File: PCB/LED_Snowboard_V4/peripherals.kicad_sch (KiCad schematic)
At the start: 16 parts, among them J1 Micro_SD_Card_Det_Hirose_DM3AT, U2 MPU-6050, U3 NEO-M8M

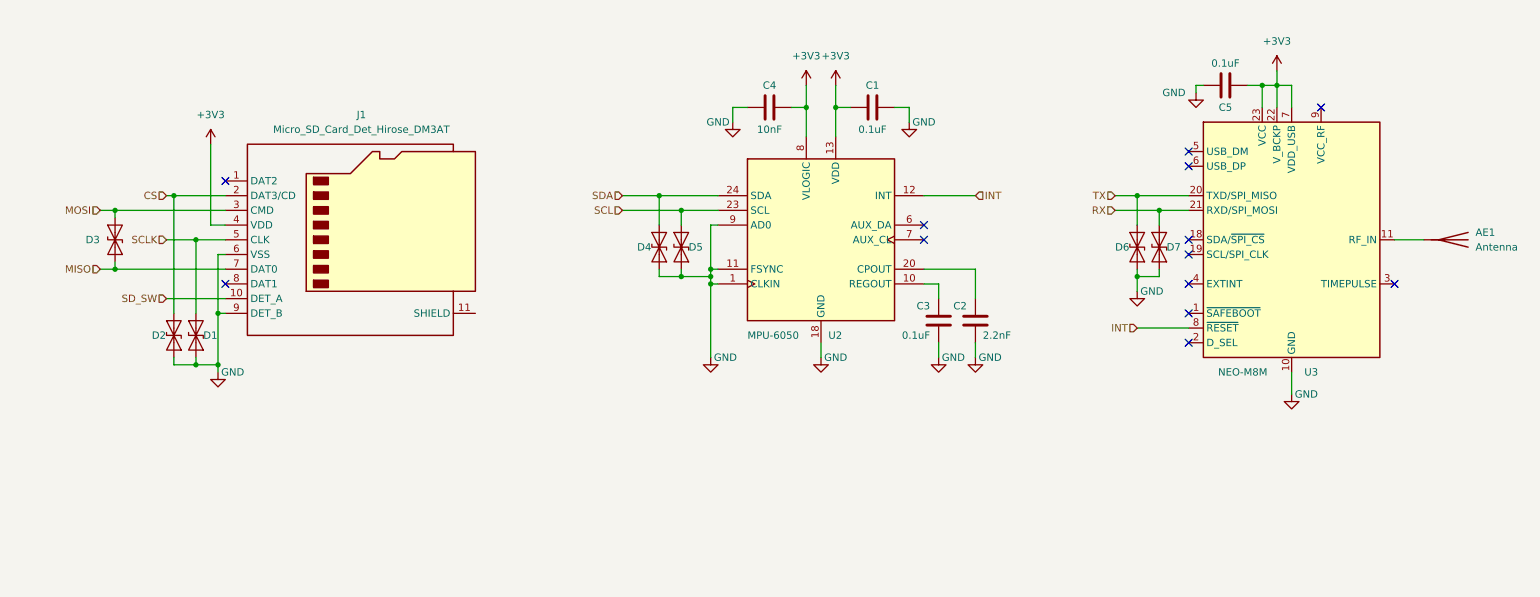
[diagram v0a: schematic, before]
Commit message: Post Review
Reviewed with Tim. need to add power line protections. settled on no battery heater for now
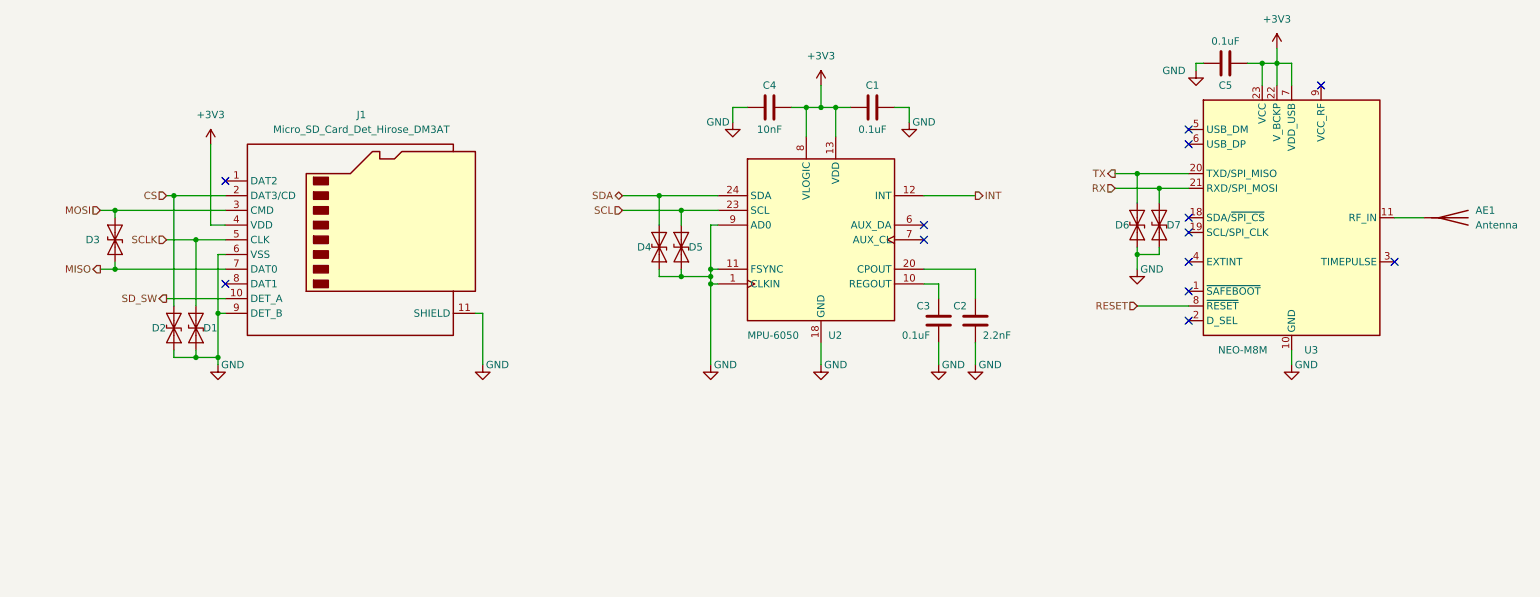
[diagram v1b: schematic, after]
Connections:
- net GND: now also J1.11 (SHIELD)
- net INT: no longer U3.8 (~{RESET})
- new net RESET: U3.8 (~{RESET})
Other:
- moved on the sheet: AE1, C5, D1, D2, D6, D7, U3

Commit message: makerfaire
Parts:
- AE1: footprint (none) -> Connector_Coaxial:U.FL_Hirose_U.FL-R-SMT-1_Vertical
- C1, C2, C3, C4, C5: footprint (none) -> Capacitor_SMD:C_0603_1608Metric_Pad1.08x0.95mm_HandSolder
- J1: footprint (none) -> Connector_Card:microSD_HC_Hirose_DM3AT-SF-PEJM5
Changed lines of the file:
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@@
       (effects (font (size 1.27 1.27)))
     )
-    (property "Footprint" "" (at 125.73 74.93 0)
+    (property "Footprint" "Connector_Card:microSD_HC_Hirose_DM3AT-SF-PEJM5" (at 125.73 74.93 0)
       (effects (font (size 1.27 1.27)) hide)
     )
@@
       (effects (font (size 1.27 1.27)))
     )
-    (property "Footprint" "" (at 148.59 68.8848 0)
+    (property "Footprint" "Capacitor_SMD:C_0603_1608Metric_Pad1.08x0.95mm_HandSolder" (at 148.59 68.8848 0)
       (effects (font (size 1.27 1.27)) hide)
     )
@@
       (effects (font (size 1.27 1.27)) (justify right))
     )
-    (property "Footprint" "" (at 179.3748 102.87 0)
+    (property "Footprint" "Capacitor_SMD:C_0603_1608Metric_Pad1.08x0.95mm_HandSolder" (at 179.3748 102.87 0)
       (effects (font (size 1.27 1.27)) hide)
     )
@@
       (effects (font (size 1.27 1.27)) (justify right))
     )
-    (property "Footprint" "" (at 173.0248 102.87 0)
+    (property "Footprint" "Capacitor_SMD:C_0603_1608Metric_Pad1.08x0.95mm_HandSolder" (at 173.0248 102.87 0)
       (effects (font (size 1.27 1.27)) hide)
     )
@@
       (effects (font (size 1.27 1.27)) (justify left))
     )
-    (property "Footprint" "" (at 262.89 88.9 0)
+    (property "Footprint" "Connector_Coaxial:U.FL_Hirose_U.FL-R-SMT-1_Vertical" (at 262.89 88.9 0)
       (effects (font (size 1.27 1.27)) hide)
     )
@@
       (effects (font (size 1.27 1.27)))
     )
-    (property "Footprint" "" (at 166.37 68.8848 0)
+    (property "Footprint" "Capacitor_SMD:C_0603_1608Metric_Pad1.08x0.95mm_HandSolder" (at 166.37 68.8848 0)
       (effects (font (size 1.27 1.27)) hide)
     )
@@
       (effects (font (size 1.27 1.27)))
     )
-    (property "Footprint" "" (at 219.71 63.1952 0)
-      (effects (font (size 1.27 1.27)) hide)
-    )
+    (property "Footprint" "Capacitor_SMD:C_0603_1608Metric_Pad1.08x0.95mm_HandSolder" (at 219.71 63.1952 0)
+      (effects (font (size 1.27 1.27)) hide)
+    )

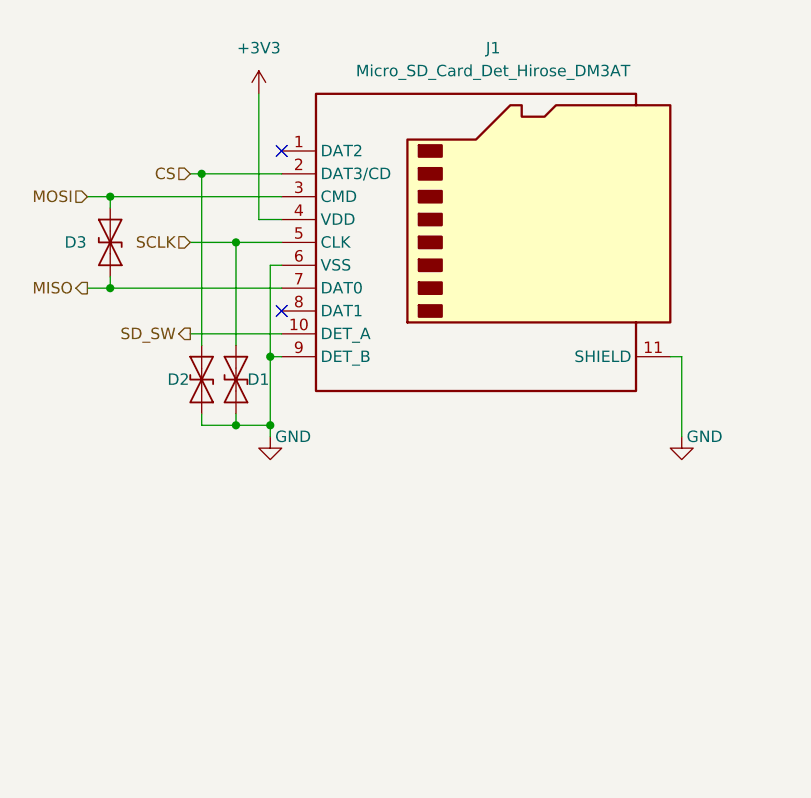
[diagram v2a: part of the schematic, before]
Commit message: Added Ram
Added Ram. need to finish DRC checks
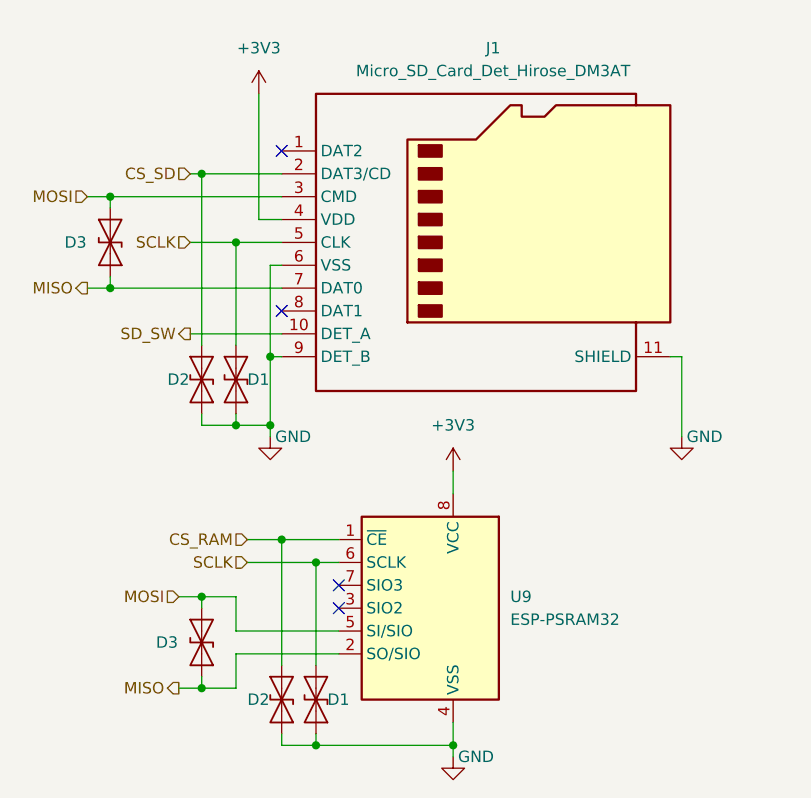
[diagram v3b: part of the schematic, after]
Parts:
- added D1, D2, D3: SD05_SOD323, Diode_SMD:D_SOD-323, symbol Diode:SD05_SOD323
- added U9: ESP-PSRAM32, Package_SO:SOIC-8_3.9x4.9mm_P1.27mm, symbol Memory_RAM:ESP-PSRAM32
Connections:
- net +3V3: now also U9.8 (VCC)
- net GND: now also D1.1 (A1), D2.1 (A1), U9.4 (VSS)
- net MISO: now also D3.1 (A1), U9.2 (SO/SIO)
- net MOSI: now also D3.2 (A2), U9.5 (SI/SIO)
- net SCLK: now also D1.2 (A2), U9.6 (SCLK)
- net CS renamed CS_SD
- new net CS_RAM: D2.2 (A2), U9.1 (~{CE})
- no-connect marks 13 -> 15

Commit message: updated control pcb
updated to add high side switching as well as added voltage divider and adjusted layout
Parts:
- removed D1, D2, D3 (x2), D4, D5, D7: SD05_SOD323, Diode_SMD:D_SOD-323, symbol Diode:SD05_SOD323
- added C21, C22: 0.1uF, Capacitor_SMD:C_0603_1608Metric_Pad1.08x0.95mm_HandSolder, symbol Device:C
- added D9: SD05_SOD323, Diode_SMD:D_SOD-323, symbol Diode:SD05_SOD323
- renumbered C4 to C12, C1 to C13, C3 to C14, C2 to C15, C5 to C16, D2 to D7, D1 to D8, J1 to J11, U2 to U7, U3 to U8
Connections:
- net +3V3: now also C21.2, C22.2
- net GND: now also C21.1, C22.1, D9.1 (A1)
- net MISO: now also D9.2 (A2)
- net MOSI: now also D6.2 (A2)
- net TX: no longer D6.2 (A2)
